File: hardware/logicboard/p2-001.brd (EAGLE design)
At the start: 72 x 72 mm, 28 parts, among them IC1 5V, IC2 74LS07N, IC3 4066N, K1 G5V1, T1 2SC1815, U1 DS18B20

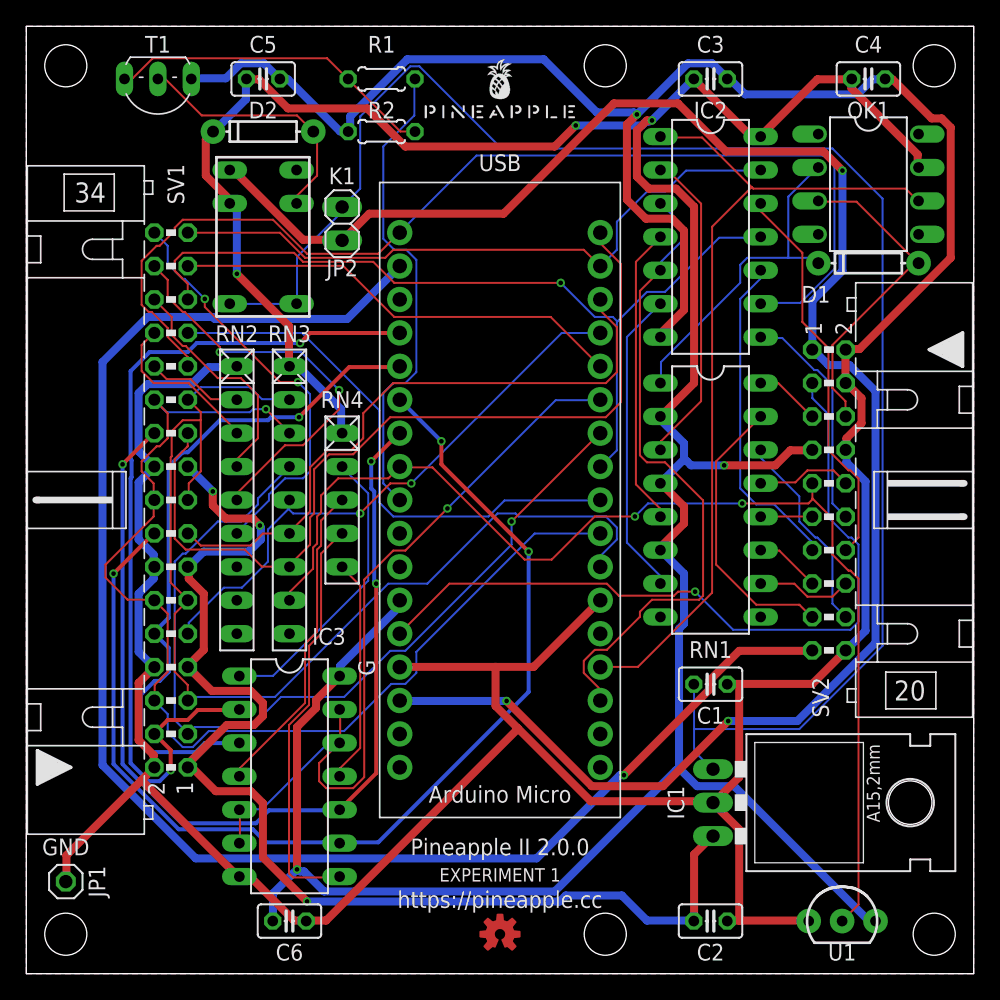
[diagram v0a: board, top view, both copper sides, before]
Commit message: Added restricted area.
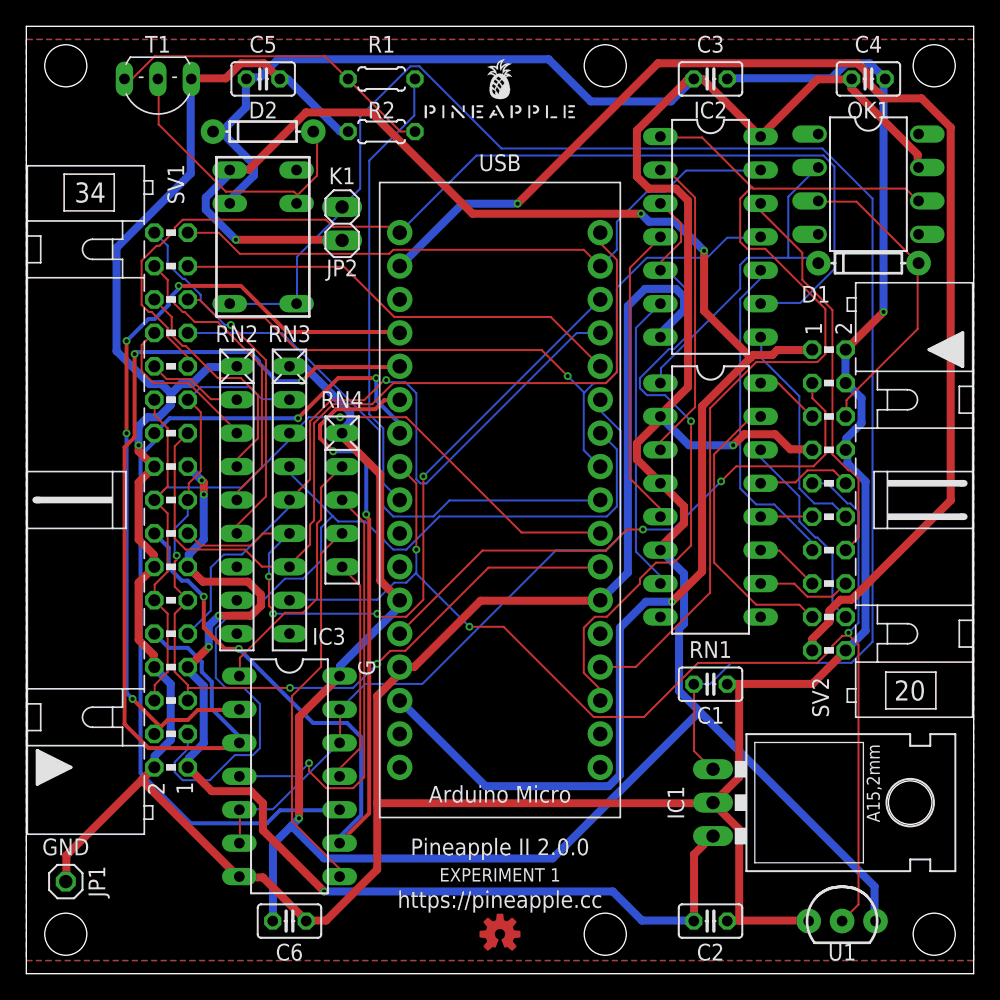
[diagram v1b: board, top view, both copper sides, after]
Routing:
- net VDD: track 120.2 -> 95.3 mm
- net A2: track 51.7 -> 71.6 mm, vias 1 -> 2
- net SCL: track 85.1 -> 65.9 mm
- net SDA: track 83.9 -> 69.2 mm, vias 0 -> 3
- net RST: track 58.1 -> 43.8 mm, vias 1 -> 2
- net D2: track 43.7 -> 56.0 mm, vias 2 -> 1
- net +12V: track 138.4 -> 128.6 mm, vias 3 -> 4
- net VCC: track 245.6 -> 254.9 mm, vias 5 -> 2
- net N$4: track 24.3 -> 33.2 mm, vias 0 -> 1
- net A4: track 75.8 -> 66.9 mm, vias 3 -> 2
- net RX: track 64.6 -> 73.4 mm
- net A3: track 83.9 -> 75.2 mm, vias 3 -> 4
- net THS: track 87.4 -> 96.1 mm, vias 2 -> 3
- net PULLUP: track 61.0 -> 52.7 mm, vias 1 -> 0
- net LED3K: track 31.3 -> 23.1 mm, vias 2 -> 0
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
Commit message: Nothing was changed except for silk.
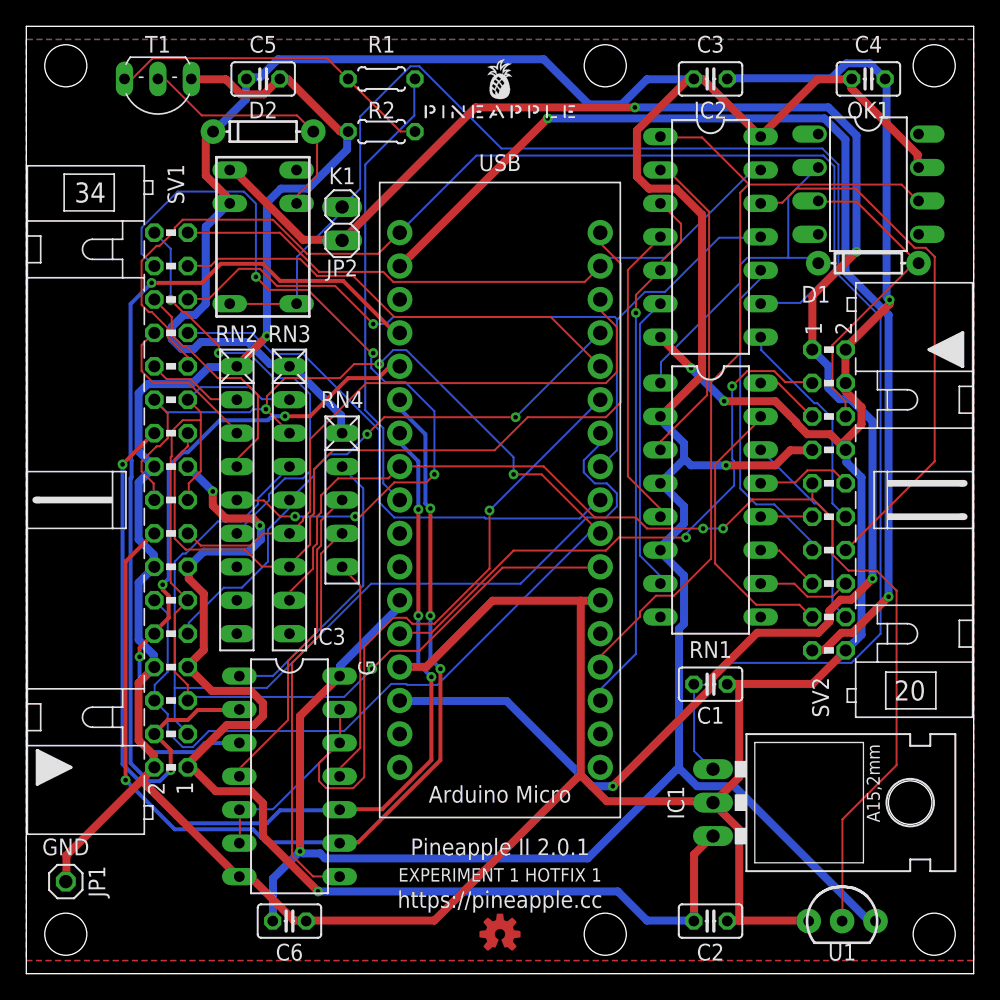
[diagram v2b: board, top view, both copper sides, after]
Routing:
- net SCL: track 65.9 -> 106.7 mm, vias 1 -> 3
- net LED3K: track 23.1 -> 59.4 mm, vias 0 -> 5
- net A2: track 71.6 -> 51.0 mm, vias 2 -> 3
- net GND: track 304.7 -> 286.3 mm, vias 2 -> 4
- net D2: track 56.0 -> 43.3 mm, vias 1 -> 2
- net VDD: track 95.3 -> 82.8 mm, vias 1 -> 2
- net A4: track 66.9 -> 79.4 mm, vias 2 -> 4
- net A1: track 62.1 -> 73.4 mm, vias 4 -> 2
- net XLEDR: track 29.9 -> 40.9 mm
- net +12V: track 128.6 -> 138.4 mm
- net RX: track 73.4 -> 63.8 mm
- net N$4: track 33.2 -> 24.3 mm, vias 1 -> 0
- net TX: track 49.9 -> 41.0 mm
- net PULLUP: track 52.7 -> 61.0 mm, vias 0 -> 1
- net D3: track 55.8 -> 47.8 mm, vias 4 -> 0
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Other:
- board text added: "EXPERIMENT 1 HOTFIX 1"
- board text added: "Pineapple II 2.0.1"
- board text removed: "EXPERIMENT 1"
- board text removed: "Pineapple II 2.0.0"

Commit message: Modified schematic and board for the better readability.
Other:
- board text added: "EXPERIMENT 1 HOTFIX 2"
- board text added: "Pineapple II 2.0.2"
- board text removed: "EXPERIMENT 1 HOTFIX 1"
- board text removed: "Pineapple II 2.0.1"
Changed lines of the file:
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@@
 <grid distance="1" unitdist="mm" unit="mm" style="dots" multiple="1" display="yes" altdistance="50" altunitdist="mil" altunit="mil"/>
 <layers>
-<layer number="1" name="Top" color="4" fill="1" visible="no" active="yes"/>
-<layer number="16" name="Bottom" color="1" fill="1" visible="no" active="yes"/>
+<layer number="1" name="Top" color="4" fill="1" visible="yes" active="yes"/>
+<layer number="16" name="Bottom" color="1" fill="1" visible="yes" active="yes"/>
 <layer number="17" name="Pads" color="2" fill="1" visible="yes" active="yes"/>
 <layer number="18" name="Vias" color="2" fill="1" visible="yes" active="yes"/>
@@
 <text x="36" y="61" size="1.27" layer="25" align="bottom-center">USB</text>
 <text x="36" y="13" size="1.27" layer="25" align="bottom-center">Arduino Micro</text>
-<text x="36" y="9" size="1.27" layer="25" align="bottom-center">Pineapple II 2.0.1</text>
+<text x="36" y="9" size="1.27" layer="25" align="bottom-center">Pineapple II 2.0.2</text>
 <text x="36" y="5" size="1.27" layer="25" align="bottom-center">https://pineapple.cc</text>
 <text x="26.5" y="23.25" size="1.27" layer="25" rot="R90" align="bottom-center">G</text>
 <text x="3" y="9" size="1.27" layer="25" align="bottom-center">GND</text>
-<text x="36" y="7" size="1.016" layer="25" align="bottom-center">EXPERIMENT 1 HOTFIX 1</text>
+<text x="36" y="7" size="1.016" layer="25" align="bottom-center">EXPERIMENT 1 HOTFIX 2</text>
 <circle x="3" y="3" radius="2.236065625" width="0.2" layer="42"/>
 <circle x="69" y="3" radius="2.236065625" width="0.2" layer="42"/>
@@
 <element name="IC3" library="40xx" library_urn="urn:adsk.eagle:library:80" package="DIL14" package3d_urn="urn:adsk.eagle:package:16407/2" value="4066N" x="20" y="15" smashed="yes" rot="R270">
 <attribute name="NAME" x="23" y="25" size="1.27" layer="25" ratio="10" align="bottom-center"/>
-<attribute name="VALUE" x="19.365" y="21.731" size="1.27" layer="27" ratio="10" rot="R270"/>
+<attribute name="VALUE" x="19" y="15" size="0.8128" layer="27" ratio="10" rot="R90" align="bottom-center"/>
 </element>
 <element name="JP2" library="pinhead" library_urn="urn:adsk.eagle:library:325" package="1X02" package3d_urn="urn:adsk.eagle:package:22435/2" value="" x="24" y="57" smashed="yes" rot="R90">
@@
 <contactref element="C4" pad="2"/>
 <contactref element="C5" pad="2"/>
-<contactref element="U1" pad="1"/>
 <contactref element="JP1" pad="1"/>
 <contactref element="C6" pad="2"/>
 <contactref element="IC3" pad="7"/>
+<contactref element="U1" pad="1"/>
 <wire x1="20.3454" y1="4.0386" x2="21.2598" y2="4.0386" width="0.6096" layer="1"/>
 <wire x1="17.0688" y1="7.3152" x2="20.3454" y2="4.0386" width="0.6096" layer="1"/>
@@
 <contactref element="C5" pad="1"/>
 <contactref element="RN3" pad="1"/>
-<contactref element="U1" pad="3"/>
 <contactref element="RN4" pad="1"/>
 <contactref element="C6" pad="1"/>
 <contactref element="IC3" pad="14"/>
+<contactref element="U1" pad="3"/>
 <wire x1="23.9268" y1="42.4434" x2="23.9268" y2="41.148" width="0.6096" layer="16"/>
 <wire x1="20.2692" y1="46.101" x2="23.9268" y2="42.4434" width="0.6096" layer="16"/>
@@
 <signal name="SCL">
 <contactref element="MC1" pad="P$10"/>
+<contactref element="RN3" pad="3"/>
 <contactref element="SV1" pad="6"/>
 <contactref element="SV1" pad="24"/>
 <contactref element="SV1" pad="18"/>
 <contactref element="SV1" pad="12"/>
-<contactref element="RN3" pad="3"/>
 <wire x1="18.2118" y1="42.9006" x2="19.9644" y2="41.148" width="0.1524" layer="1"/>
 <wire x1="17.2212" y1="42.9006" x2="18.2118" y2="42.9006" width="0.1524" layer="16"/>
@@
 <signal name="THS">
 <contactref element="MC1" pad="P$27"/>
+<contactref element="SV2" pad="9"/>
 <contactref element="U1" pad="2"/>
 <contactref element="RN3" pad="8"/>
-<contactref element="SV2" pad="9"/>
 <wire x1="20.0406" y1="29.0322" x2="20.0406" y2="28.4226" width="0.1524" layer="1"/>
 <wire x1="21.7932" y1="30.7848" x2="20.0406" y2="29.0322" width="0.1524" layer="1"/>

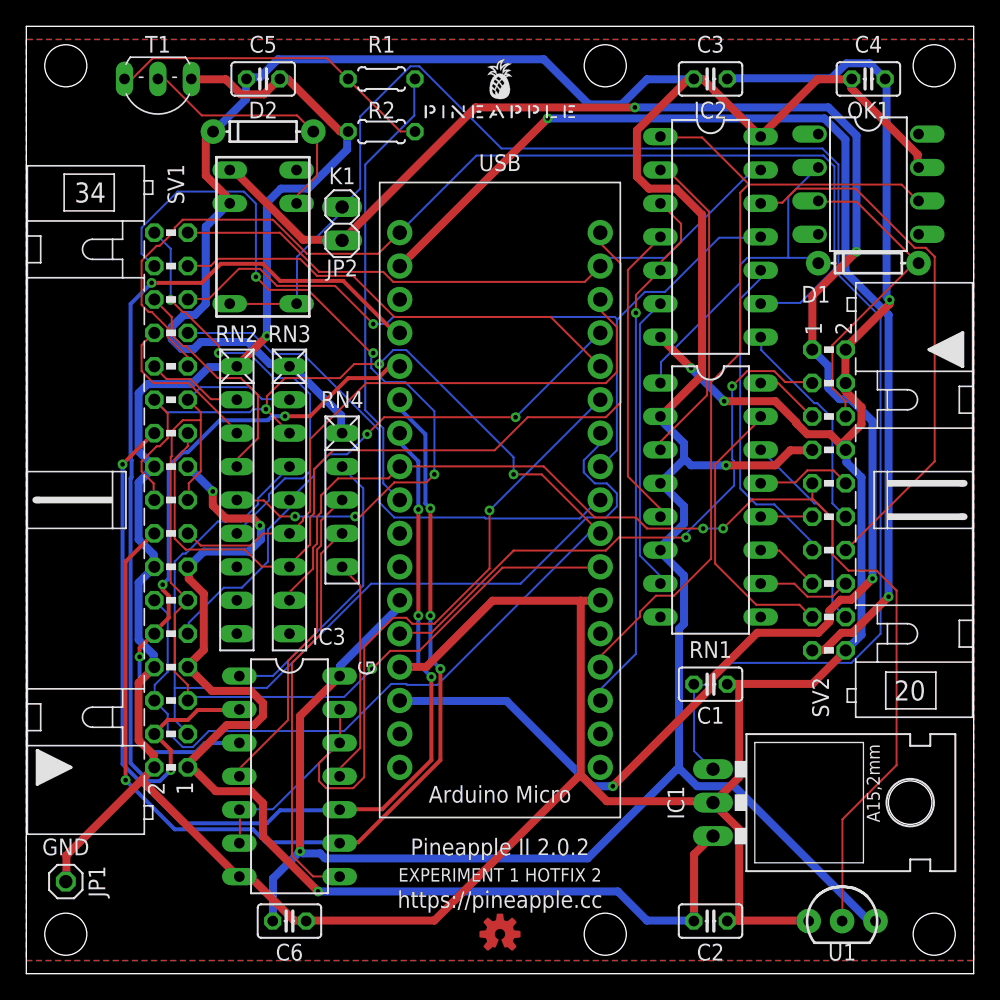
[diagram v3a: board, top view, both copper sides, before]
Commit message: Real hotfix! Now pull-ups to Analog In are connected to Vout, not Vcc.
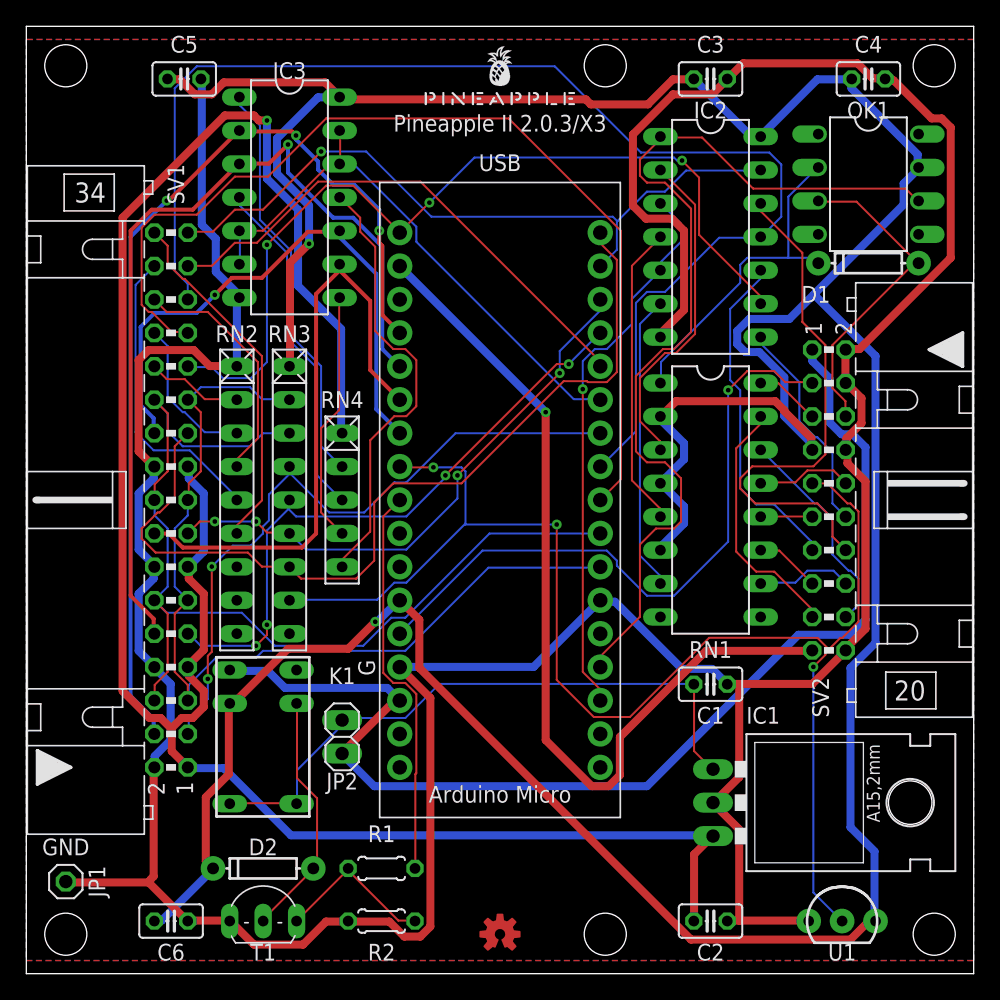
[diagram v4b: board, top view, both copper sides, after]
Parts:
- moved T1 64.5 mm to (18.0, 4.00), turned to 0 degrees
- moved R1 60.0 mm to (27.0, 8.00)
- moved R2 60.0 mm to (27.0, 4.00)
- moved D2 56.0 mm to (18.0, 8.00)
- moved IC3 44.0 mm to (20.0, 59.0)
- moved JP2 39.0 mm to (24.0, 18.0)
- moved K1 38.0 mm to (18.0, 18.0)
- moved C6 9.00 mm to (11.0, 4.00)
- moved C5 6.00 mm to (12.0, 68.0)
- moved U$1 1.00 mm to (36.0, 66.0)
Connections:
- net VCC: no longer RN4.1
- net VOUT: now also RN4.1
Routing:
- net 12VRLY: track 122.2 -> 47.9 mm
- net VOUT: track 91.3 -> 157.9 mm, vias 3 -> 1
- net +12V: track 138.4 -> 88.7 mm, vias 4 -> 0
- net LED2: track 60.9 -> 97.7 mm, vias 1 -> 0
- net LED3K: track 59.4 -> 23.2 mm, vias 5 -> 0
- net A4: track 79.4 -> 43.9 mm, vias 4 -> 1
- net LED1: track 41.0 -> 74.8 mm
- net VCC: track 255.8 -> 287.6 mm
- net A3: track 76.9 -> 46.6 mm, vias 4 -> 0
- net SCL: track 106.7 -> 77.2 mm, vias 3 -> 0
- net D1: track 72.5 -> 52.2 mm, vias 0 -> 2
- net PULLUP: track 61.0 -> 42.8 mm, vias 1 -> 0
- net THS: track 89.0 -> 106.4 mm, vias 2 -> 3
- net N$6: track 17.2 -> 33.9 mm
- net A2: track 51.0 -> 67.3 mm, vias 3 -> 1
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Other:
- board text added: "Pineapple II 2.0.3/X3"
- board text removed: "EXPERIMENT 1 HOTFIX 2"
- board text removed: "Pineapple II 2.0.2"
- board text removed: "https://pineapple.cc"

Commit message: Added pull-up selector.
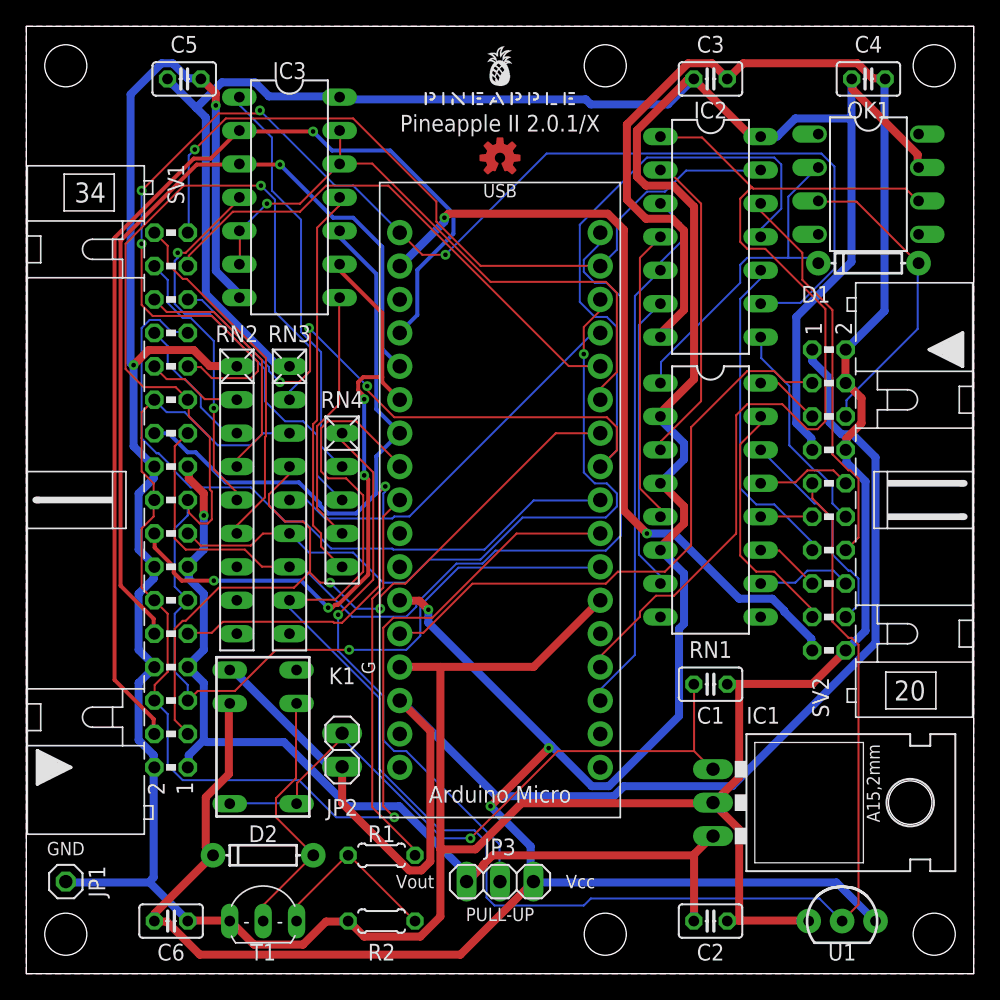
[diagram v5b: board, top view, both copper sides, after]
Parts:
- added JP3: (no value), pinhead:1X03
- moved LOGO1 59.0 mm to (36.0, 62.0)
- moved D2 1.00 mm to (18.0, 9.00)
- moved JP2 1.00 mm to (24.0, 17.0)
- moved R1 1.00 mm to (27.0, 9.00)
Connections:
- net 12VRLY renamed N$1
- new net N$2: JP3.2, RN4.1
- net VCC: now also JP3.3
- net VOUT: now also JP3.1; no longer RN4.1
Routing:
- net VOUT: track 157.9 -> 75.9 mm
- net SDA: track 70.1 -> 112.7 mm, vias 0 -> 2
- net N$2: track 0.00 -> 41.8 mm, vias 0 -> 1
- net LED0: track 66.5 -> 103.7 mm, vias 3 -> 4
- net GND: track 285.4 -> 313.9 mm, vias 0 -> 2
- net LED1: track 74.8 -> 52.6 mm
- net SCL: track 77.2 -> 95.8 mm, vias 0 -> 1
- net +12V: track 88.7 -> 105.5 mm
- net THS: track 106.4 -> 121.1 mm, vias 3 -> 0
- net VCC: track 287.6 -> 300.6 mm, vias 2 -> 3
- net D3: track 43.0 -> 55.1 mm, vias 4 -> 1
- net XLEDR: track 39.9 -> 29.9 mm
- net D2: track 47.5 -> 56.4 mm, vias 4 -> 1
- net VDD: track 68.3 -> 59.9 mm, vias 1 -> 2
- net D1: track 52.2 -> 60.5 mm
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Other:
- board text added: "PULL-UP"
- board text added: "Pineapple II 2.0.1/X"
- board text added: "Vcc"
- board text added: "Vout"
- board text removed: "Pineapple II 2.0.3/X3"
